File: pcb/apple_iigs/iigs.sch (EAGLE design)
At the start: 16 parts, among them J1 ATX24RH

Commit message: added iigs
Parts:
- removed C1, C2: (no value), capacitor-wima:C5/2.5
- removed JP3: (no value), appleii:4PIN_FAN
- removed U$3: ROCK_SW, atx4vc:ROCK_SW
- removed U$6: APPLEII, atx4vc:APPLEII
- added JP2: (no value), pinhead:PINHD-1X3
- J1: device macse:ATX24RH -> appleii:ATX24RH
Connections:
- new net N$1: JP2.2, JP4.2_VCC
- net +12V: now also JP2.3; no longer JP3.2_VCC, U$6.P$4
- net +5V: now also JP2.1; no longer JP4.2_VCC, U$6.P$3
- net -12V: no longer U$6.P$5
- net -5V: no longer U$6.P$6
- net GND: no longer C1.2, C2.2, JP3.1_GND, U$3.P$1, U$3.P$3, U$6.P$1, U$6.P$2
- net N$5: no longer U$3.P$2, U$3.P$4
- net N$6: no longer C1.1
- net N$8: no longer C2.1

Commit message: updated IIGS design
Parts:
- removed J7: (no value), atx_power_control:CONN_023.5MM-NO_SILK
- removed U$4, U$5: M2.5_MOUNTING_HOLE, appleii:M2.5_MOUNTING_HOLE
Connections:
- net GND: no longer J7.2
- net N$5: no longer J7.1
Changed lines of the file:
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@@
 <part name="GND3" library="supply1" library_urn="urn:adsk.eagle:library:371" deviceset="GND" device=""/>
 <part name="J1" library="appleii" deviceset="ATX24" device="RH"/>
-<part name="U$5" library="appleii" deviceset="M2.5_MOUNTING_HOLE" device=""/>
-<part name="U$4" library="appleii" deviceset="M2.5_MOUNTING_HOLE" device=""/>
 <part name="IC1" library="v-reg" library_urn="urn:adsk.eagle:library:409" deviceset="79XXS" device="" package3d_urn="urn:adsk.eagle:package:30343/1"/>
 <part name="GND5" library="supply1" library_urn="urn:adsk.eagle:library:371" deviceset="GND" device=""/>
@@
 <part name="P-7" library="supply1" library_urn="urn:adsk.eagle:library:371" deviceset="-12V" device=""/>
 <part name="JP4" library="appleii" deviceset="4PIN_FAN" device=""/>
-<part name="J7" library="atx_power_control" deviceset="CONN_02" device="3.5MM-NO_SILK"/>
 <part name="JP2" library="pinhead" library_urn="urn:adsk.eagle:library:325" deviceset="PINHD-1X3" device="" package3d_urn="urn:adsk.eagle:package:22458/2"/>
 <part name="GND1" library="supply1" library_urn="urn:adsk.eagle:library:371" deviceset="GND" device=""/>
@@
 <attribute name="VALUE" x="83.82" y="149.86" size="1.27" layer="96"/>
 </instance>
-<instance part="U$5" gate="G$1" x="88.9" y="121.92" smashed="yes"/>
-<instance part="U$4" gate="G$1" x="66.04" y="121.92" smashed="yes"/>
 <instance part="IC1" gate="1" x="147.32" y="96.52" smashed="yes">
 <attribute name="NAME" x="149.86" y="105.41" size="1.778" layer="95"/>
@@
 </instance>
 <instance part="JP4" gate="A" x="-17.78" y="175.26" smashed="yes"/>
-<instance part="J7" gate="G$1" x="200.66" y="162.56" smashed="yes" rot="R180">
-<attribute name="VALUE" x="203.2" y="167.386" size="1.778" layer="96" font="vector" rot="R180"/>
-<attribute name="NAME" x="203.2" y="156.972" size="1.778" layer="95" font="vector" rot="R180"/>
-</instance>
 <instance part="JP2" gate="A" x="0" y="177.8" smashed="yes">
 <attribute name="NAME" x="-6.35" y="183.515" size="1.778" layer="95"/>
@@
 <pinref part="JP1" gate="G$1" pin="2"/>
 <wire x1="149.86" y1="160.02" x2="177.8" y2="160.02" width="0.1524" layer="91"/>
-<wire x1="177.8" y1="160.02" x2="193.04" y2="160.02" width="0.1524" layer="91"/>
-<junction x="177.8" y="160.02"/>
-<pinref part="J7" gate="G$1" pin="2"/>
 </segment>
 <segment>
@@
 <pinref part="JP1" gate="G$1" pin="1"/>
 <pinref part="J1" gate="G$1" pin="PS_ON"/>
-<wire x1="177.8" y1="162.56" x2="193.04" y2="162.56" width="0.1524" layer="91"/>
-<junction x="177.8" y="162.56"/>
-<pinref part="J7" gate="G$1" pin="1"/>
-</segment>
-</net>
+</segment>
+</net>

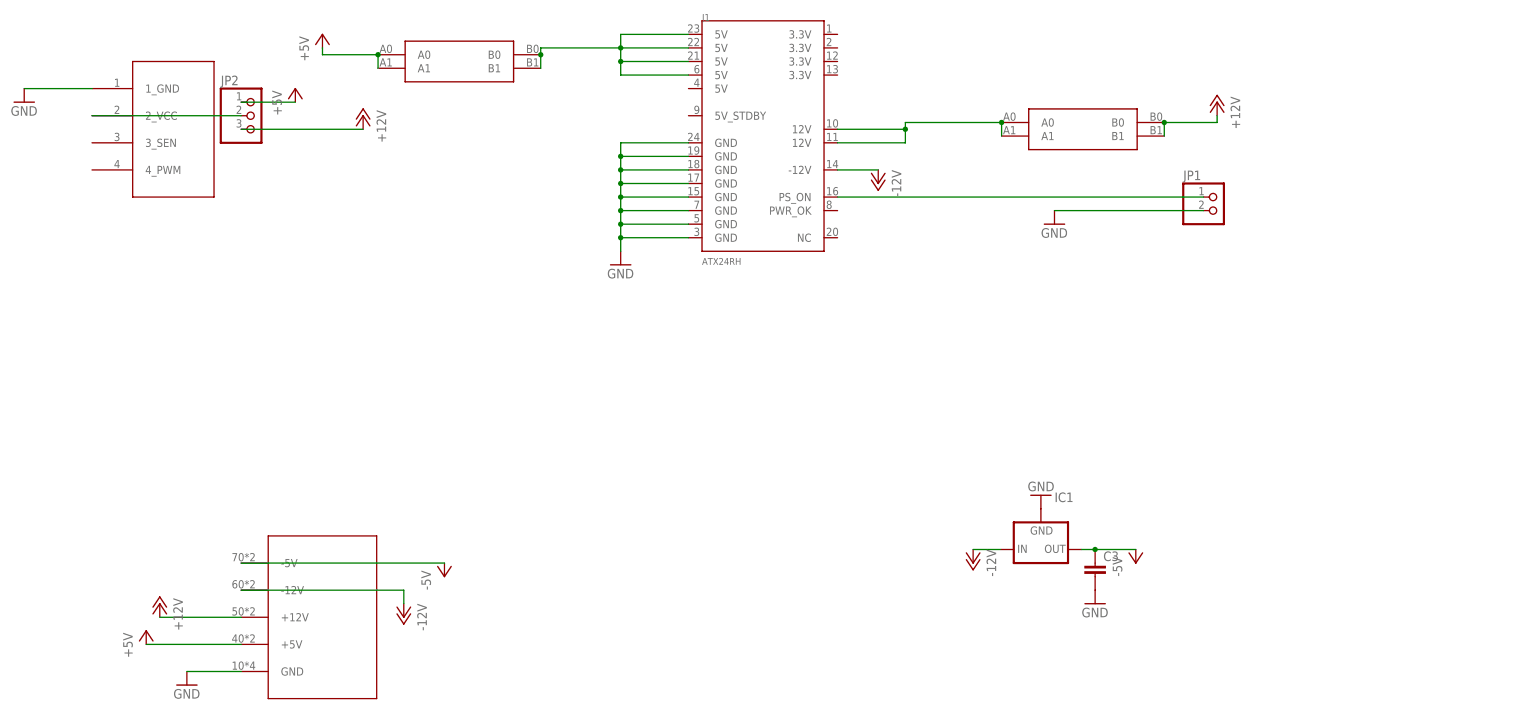
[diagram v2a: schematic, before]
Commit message: changed to 70L05
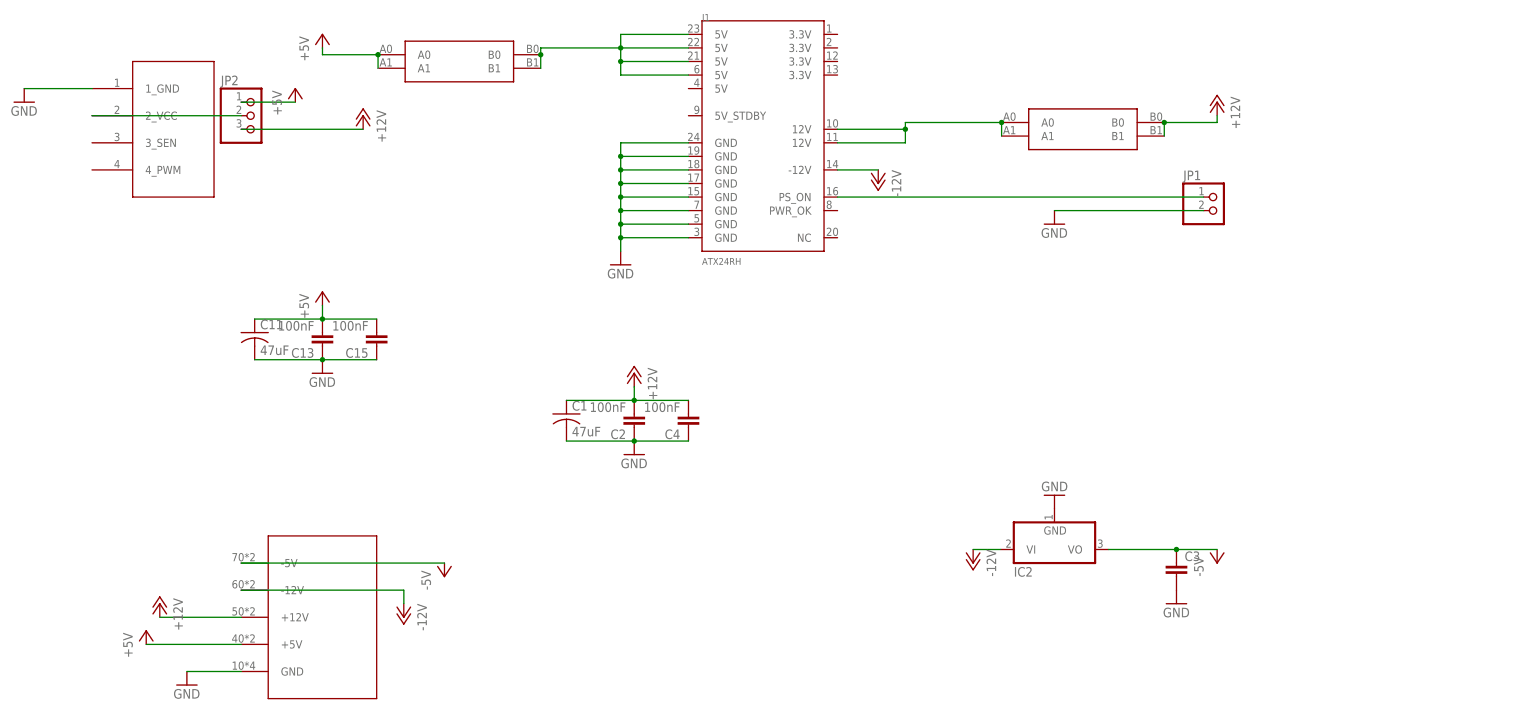
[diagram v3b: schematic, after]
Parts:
- removed IC1: (no value), v-reg:79XXS
- added C1, C11: 47uF, clock:C-USC1210
- added C13, C15, C2, C4: 100nF, clock:CAP0805
- added IC2: (no value), linear:7905L
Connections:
- net +12V: now also C1.1, C2.2, C4.2
- net +5V: now also C11.1, C13.2, C15.2
- net -12V: now also IC2.VI; no longer IC1.IN
- net -5V: now also IC2.VO; no longer IC1.OUT
- net GND: now also C1.2, C11.2, C13.1, C15.1, C2.1, C4.1, IC2.GND; no longer IC1.GND
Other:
- moved on the sheet: C3
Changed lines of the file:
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@@
 <?xml version="1.0" encoding="utf-8"?>
 <!DOCTYPE eagle SYSTEM "eagle.dtd">
-<eagle version="9.6.1">
+<eagle version="9.6.2">
 <drawing>
 <settings>
@@
 <part name="GND3" library="supply1" library_urn="urn:adsk.eagle:library:371" deviceset="GND" device=""/>
 <part name="J1" library="appleii" deviceset="ATX24" device="RH"/>
-<part name="IC1" library="v-reg" library_urn="urn:adsk.eagle:library:409" deviceset="79XXS" device="" package3d_urn="urn:adsk.eagle:package:30343/1"/>
 <part name="GND5" library="supply1" library_urn="urn:adsk.eagle:library:371" deviceset="GND" device=""/>
 <part name="P-3" library="supply1" library_urn="urn:adsk.eagle:library:371" deviceset="-12V" device=""/>
@@
 <part name="P+1" library="supply1" library_urn="urn:adsk.eagle:library:371" deviceset="+5V" device=""/>
 <part name="P+4" library="supply1" library_urn="urn:adsk.eagle:library:371" deviceset="+12V" device=""/>
+<part name="IC2" library="linear" library_urn="urn:adsk.eagle:library:262" deviceset="79*" device="L" package3d_urn="urn:adsk.eagle:package:16416/2" technology="05"/>
+<part name="C11" library="clock" deviceset="C-US" device="C1210" value="47uF"/>
+<part name="C13" library="clock" deviceset="CAP" device="0805" value="100nF"/>
+<part name="C15" library="clock" deviceset="CAP" device="0805" value="100nF"/>
+<part name="P+5" library="supply1" library_urn="urn:adsk.eagle:library:371" deviceset="+5V" device=""/>
+<part name="GND6" library="supply1" library_urn="urn:adsk.eagle:library:371" deviceset="GND" device=""/>
+<part name="C1" library="clock" deviceset="C-US" device="C1210" value="47uF"/>
+<part name="C2" library="clock" deviceset="CAP" device="0805" value="100nF"/>
+<part name="C4" library="clock" deviceset="CAP" device="0805" value="100nF"/>
+<part name="GND7" library="supply1" library_urn="urn:adsk.eagle:library:371" deviceset="GND" device=""/>
+<part name="P+8" library="supply1" library_urn="urn:adsk.eagle:library:371" deviceset="+12V" device=""/>
 </parts>
 <sheets>
@@
 <attribute name="VALUE" x="83.82" y="149.86" size="1.27" layer="96"/>
 </instance>
-<instance part="IC1" gate="1" x="147.32" y="96.52" smashed="yes">
-<attribute name="NAME" x="149.86" y="105.41" size="1.778" layer="95"/>
-<attribute name="VALUE" x="149.86" y="102.87" size="1.778" layer="96"/>
-</instance>
-<instance part="GND5" gate="1" x="147.32" y="106.68" smashed="yes" rot="R180">
-<attribute name="VALUE" x="149.86" y="109.22" size="1.778" layer="96" rot="R180"/>
+<instance part="GND5" gate="1" x="149.86" y="106.68" smashed="yes" rot="R180">
+<attribute name="VALUE" x="152.4" y="109.22" size="1.778" layer="96" rot="R180"/>
 </instance>
 <instance part="P-3" gate="1" x="134.62" y="93.98" smashed="yes" rot="MR0">
 <attribute name="VALUE" x="137.16" y="91.44" size="1.778" layer="96" rot="MR90"/>
 </instance>
-<instance part="P-4" gate="1" x="165.1" y="93.98" smashed="yes">
-<attribute name="VALUE" x="162.56" y="91.44" size="1.778" layer="96" rot="R90"/>
-</instance>
-<instance part="C3" gate="G$1" x="157.48" y="93.98" smashed="yes">
-<attribute name="NAME" x="159.004" y="94.361" size="1.778" layer="95"/>
-<attribute name="VALUE" x="159.004" y="89.281" size="1.778" layer="96"/>
-</instance>
-<instance part="GND11" gate="1" x="157.48" y="86.36" smashed="yes">
-<attribute name="VALUE" x="154.94" y="83.82" size="1.778" layer="96"/>
+<instance part="P-4" gate="1" x="180.34" y="93.98" smashed="yes">
+<attribute name="VALUE" x="177.8" y="91.44" size="1.778" layer="96" rot="R90"/>
+</instance>
+<instance part="C3" gate="G$1" x="172.72" y="93.98" smashed="yes">
+<attribute name="NAME" x="174.244" y="94.361" size="1.778" layer="95"/>
+<attribute name="VALUE" x="174.244" y="89.281" size="1.778" layer="96"/>
+</instance>
+<instance part="GND11" gate="1" x="172.72" y="86.36" smashed="yes">
+<attribute name="VALUE" x="170.18" y="83.82" size="1.778" layer="96"/>
 </instance>
 <instance part="U$7" gate="G$1" x="10.16" y="83.82" smashed="yes"/>
@@
 <instance part="P+4" gate="1" x="20.32" y="177.8" smashed="yes" rot="MR0">
 <attribute name="VALUE" x="22.86" y="172.72" size="1.778" layer="96" rot="MR90"/>
+</instance>
+<instance part="IC2" gate="A1" x="149.86" y="99.06" smashed="yes">
+<attribute name="NAME" x="142.24" y="91.44" size="1.778" layer="95"/>
+<attribute name="VALUE" x="142.24" y="88.9" size="1.778" layer="96"/>
+</instance>
+<instance part="C11" gate="G$1" x="0" y="137.16" smashed="yes">
+<attribute name="NAME" x="1.016" y="137.795" size="1.778" layer="95"/>
+<attribute name="VALUE" x="1.016" y="132.969" size="1.778" layer="96"/>
+</instance>
+<instance part="C13" gate="G$1" x="12.7" y="137.16" smashed="yes" rot="R180">
+<attribute name="NAME" x="11.176" y="134.239" size="1.778" layer="95" rot="R180"/>
+<attribute name="VALUE" x="11.176" y="139.319" size="1.778" layer="96" rot="R180"/>
+</instance>
+<instance part="C15" gate="G$1" x="22.86" y="137.16" smashed="yes" rot="R180">
+<attribute name="NAME" x="21.336" y="134.239" size="1.778" layer="95" rot="R180"/>
+<attribute name="VALUE" x="21.336" y="139.319" size="1.778" layer="96" rot="R180"/>
+</instance>
+<instance part="P+5" gate="1" x="12.7" y="144.78" smashed="yes">
+<attribute name="VALUE" x="10.16" y="139.7" size="1.778" layer="96" rot="R90"/>
+</instance>
+<instance part="GND6" gate="1" x="12.7" y="129.54" smashed="yes">
+<attribute name="VALUE" x="10.16" y="127" size="1.778" layer="96"/>
+</instance>
+<instance part="C1" gate="G$1" x="58.42" y="121.92" smashed="yes">
+<attribute name="NAME" x="59.436" y="122.555" size="1.778" layer="95"/>
+<attribute name="VALUE" x="59.436" y="117.729" size="1.778" layer="96"/>
+</instance>
+<instance part="C2" gate="G$1" x="71.12" y="121.92" smashed="yes" rot="R180">
+<attribute name="NAME" x="69.596" y="118.999" size="1.778" layer="95" rot="R180"/>
+<attribute name="VALUE" x="69.596" y="124.079" size="1.778" layer="96" rot="R180"/>
+</instance>
+<instance part="C4" gate="G$1" x="81.28" y="121.92" smashed="yes" rot="R180">
+<attribute name="NAME" x="79.756" y="118.999" size="1.778" layer="95" rot="R180"/>
+<attribute name="VALUE" x="79.756" y="124.079" size="1.778" layer="96" rot="R180"/>
+</instance>
+<instance part="GND7" gate="1" x="71.12" y="114.3" smashed="yes">
+<attribute name="VALUE" x="68.58" y="111.76" size="1.778" layer="96"/>
+</instance>
+<instance part="P+8" gate="1" x="71.12" y="129.54" smashed="yes" rot="MR0">
+<attribute name="VALUE" x="73.66" y="124.46" size="1.778" layer="96" rot="MR90"/>
 </instance>
 </instances>
@@
 </segment>
 <segment>
-<pinref part="IC1" gate="1" pin="GND"/>
-<pinref part="GND5" gate="1" pin="GND"/>
-</segment>
-<segment>
 <pinref part="C3" gate="G$1" pin="2"/>
 <pinref part="GND11" gate="1" pin="GND"/>
@@
 <wire x1="-43.18" y1="182.88" x2="-30.48" y2="182.88" width="0.1524" layer="91"/>
 </segment>
+<segment>
+<pinref part="IC2" gate="A1" pin="GND"/>
+<pinref part="GND5" gate="1" pin="GND"/>
+</segment>
+<segment>
+<pinref part="C15" gate="G$1" pin="1"/>
+<pinref part="C13" gate="G$1" pin="1"/>
+<wire x1="22.86" y1="132.08" x2="12.7" y2="132.08" width="0.1524" layer="91"/>
+<pinref part="C11" gate="G$1" pin="2"/>
+<wire x1="12.7" y1="132.08" x2="0" y2="132.08" width="0.1524" layer="91"/>
+<junction x="12.7" y="132.08"/>
+<pinref part="GND6" gate="1" pin="GND"/>
+</segment>
+<segment>
+<pinref part="C4" gate="G$1" pin="1"/>
+<pinref part="C2" gate="G$1" pin="1"/>
+<wire x1="81.28" y1="116.84" x2="71.12" y2="116.84" width="0.1524" layer="91"/>
+<pinref part="C1" gate="G$1" pin="2"/>
+<wire x1="71.12" y1="116.84" x2="58.42" y2="116.84" width="0.1524" layer="91"/>
+<junction x="71.12" y="116.84"/>
+<pinref part="GND7" gate="1" pin="GND"/>
+</segment>
 </net>
 <net name="-12V" class="0">
@@
 <segment>
 <pinref part="P-3" gate="1" pin="-12V"/>
-<pinref part="IC1" gate="1" pin="IN"/>
 <wire x1="134.62" y1="96.52" x2="139.7" y2="96.52" width="0.1524" layer="91"/>
+<pinref part="IC2" gate="A1" pin="VI"/>
 </segment>
 <segment>
@@
 <wire x1="-2.54" y1="180.34" x2="7.62" y2="180.34" width="0.1524" layer="91"/>
 </segment>
+<segment>
+<pinref part="C11" gate="G$1" pin="1"/>
+<pinref part="C13" gate="G$1" pin="2"/>
+<wire x1="0" y1="139.7" x2="12.7" y2="139.7" width="0.1524" layer="91"/>
+<pinref part="C15" gate="G$1" pin="2"/>
+<wire x1="12.7" y1="139.7" x2="22.86" y2="139.7" width="0.1524" layer="91"/>
+<junction x="12.7" y="139.7"/>
+<pinref part="P+5" gate="1" pin="+5V"/>
+<wire x1="12.7" y1="142.24" x2="12.7" y2="139.7" width="0.1524" layer="91"/>
+</segment>
 </net>
 <net name="N$8" class="0">
@@
 <wire x1="-2.54" y1="175.26" x2="20.32" y2="175.26" width="0.1524" layer="91"/>
 </segment>
+<segment>
+<pinref part="C1" gate="G$1" pin="1"/>
+<pinref part="C2" gate="G$1" pin="2"/>
+<wire x1="58.42" y1="124.46" x2="71.12" y2="124.46" width="0.1524" layer="91"/>
+<pinref part="C4" gate="G$1" pin="2"/>
+<wire x1="71.12" y1="124.46" x2="81.28" y2="124.46" width="0.1524" layer="91"/>
+<junction x="71.12" y="124.46"/>
+<wire x1="71.12" y1="127" x2="71.12" y2="124.46" width="0.1524" layer="91"/>
+<pinref part="P+8" gate="1" pin="+12V"/>
+</segment>
 </net>
 <net name="N$5" class="0">
@@
 <net name="-5V" class="0">
 <segment>
-<pinref part="IC1" gate="1" pin="OUT"/>
 <pinref part="P-4" gate="1" pin="-5V"/>
-<wire x1="154.94" y1="96.52" x2="157.48" y2="96.52" width="0.1524" layer="91"/>
 <pinref part="C3" gate="G$1" pin="1"/>
-<wire x1="157.48" y1="96.52" x2="165.1" y2="96.52" width="0.1524" layer="91"/>
-<junction x="157.48" y="96.52"/>
-</segment>
-<segment>
+<wire x1="172.72" y1="96.52" x2="180.34" y2="96.52" width="0.1524" layer="91"/>
+<pinref part="IC2" gate="A1" pin="VO"/>
+<wire x1="160.02" y1="96.52" x2="172.72" y2="96.52" width="0.1524" layer="91"/>
+<junction x="172.72" y="96.52"/>
+</segment>
+<segment>

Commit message: switched back to 7905
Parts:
- removed IC2: (no value), linear:7905L
- added IC1: (no value), v-reg:79XXS
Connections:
- net -12V: now also IC1.IN; no longer IC2.VI
- net -5V: now also IC1.OUT; no longer IC2.VO
- net GND: now also IC1.GND; no longer IC2.GND
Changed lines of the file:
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@@
 <part name="P+1" library="supply1" library_urn="urn:adsk.eagle:library:371" deviceset="+5V" device=""/>
 <part name="P+4" library="supply1" library_urn="urn:adsk.eagle:library:371" deviceset="+12V" device=""/>
-<part name="IC2" library="linear" library_urn="urn:adsk.eagle:library:262" deviceset="79*" device="L" package3d_urn="urn:adsk.eagle:package:16416/2" technology="05"/>
 <part name="C11" library="clock" deviceset="C-US" device="C1210" value="47uF"/>
 <part name="C13" library="clock" deviceset="CAP" device="0805" value="100nF"/>
@@
 <part name="GND7" library="supply1" library_urn="urn:adsk.eagle:library:371" deviceset="GND" device=""/>
 <part name="P+8" library="supply1" library_urn="urn:adsk.eagle:library:371" deviceset="+12V" device=""/>
+<part name="IC1" library="v-reg" library_urn="urn:adsk.eagle:library:409" deviceset="79XXS" device="" package3d_urn="urn:adsk.eagle:package:30343/1"/>
 </parts>
 <sheets>
@@
 <attribute name="VALUE" x="22.86" y="172.72" size="1.778" layer="96" rot="MR90"/>
 </instance>
-<instance part="IC2" gate="A1" x="149.86" y="99.06" smashed="yes">
-<attribute name="NAME" x="142.24" y="91.44" size="1.778" layer="95"/>
-<attribute name="VALUE" x="142.24" y="88.9" size="1.778" layer="96"/>
-</instance>
 <instance part="C11" gate="G$1" x="0" y="137.16" smashed="yes">
 <attribute name="NAME" x="1.016" y="137.795" size="1.778" layer="95"/>
@@
 <instance part="P+8" gate="1" x="71.12" y="129.54" smashed="yes" rot="MR0">
 <attribute name="VALUE" x="73.66" y="124.46" size="1.778" layer="96" rot="MR90"/>
+</instance>
+<instance part="IC1" gate="1" x="149.86" y="96.52" smashed="yes">
+<attribute name="NAME" x="152.4" y="105.41" size="1.778" layer="95"/>
+<attribute name="VALUE" x="152.4" y="102.87" size="1.778" layer="96"/>
 </instance>
 </instances>
@@
 </segment>
 <segment>
-<pinref part="IC2" gate="A1" pin="GND"/>
-<pinref part="GND5" gate="1" pin="GND"/>
-</segment>
-<segment>
 <pinref part="C15" gate="G$1" pin="1"/>
 <pinref part="C13" gate="G$1" pin="1"/>
@@
 <pinref part="GND7" gate="1" pin="GND"/>
 </segment>
+<segment>
+<pinref part="IC1" gate="1" pin="GND"/>
+<pinref part="GND5" gate="1" pin="GND"/>
+</segment>
 </net>
 <net name="-12V" class="0">
@@
 <segment>
 <pinref part="P-3" gate="1" pin="-12V"/>
-<wire x1="134.62" y1="96.52" x2="139.7" y2="96.52" width="0.1524" layer="91"/>
-<pinref part="IC2" gate="A1" pin="VI"/>
+<wire x1="134.62" y1="96.52" x2="142.24" y2="96.52" width="0.1524" layer="91"/>
+<pinref part="IC1" gate="1" pin="IN"/>
 </segment>
 <segment>
@@
 <pinref part="C3" gate="G$1" pin="1"/>
 <wire x1="172.72" y1="96.52" x2="180.34" y2="96.52" width="0.1524" layer="91"/>
-<pinref part="IC2" gate="A1" pin="VO"/>
-<wire x1="160.02" y1="96.52" x2="172.72" y2="96.52" width="0.1524" layer="91"/>
+<wire x1="157.48" y1="96.52" x2="172.72" y2="96.52" width="0.1524" layer="91"/>
 <junction x="172.72" y="96.52"/>
-</segment>
-<segment>
+<pinref part="IC1" gate="1" pin="OUT"/>
+</segment>
+<segment>
